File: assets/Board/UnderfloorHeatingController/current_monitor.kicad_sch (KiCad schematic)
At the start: 15 parts, among them U1 BL0937B

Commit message: Fully routed board.
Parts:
- added C19: 0.1uF, Capacitor_SMD:C_0805_2012Metric_Pad1.18x1.45mm_HandSolder, symbol Device:C
- added C20: 10uF, Capacitor_SMD:C_0805_2012Metric_Pad1.18x1.45mm_HandSolder, symbol Device:C
- C2, C4, C6: value 68n -> 68nF
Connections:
- net +3V3: now also C19.1, C20.1
- net GND: now also C19.2, C20.2
- net POWER_N: now also R11.4; no longer R11.1, R11.2, R2.1
- net POWER_N_MON: now also R11.1; no longer R11.3, R11.4, R3.1
- net at C4.2, R3.2: now also U1.3 (IN); no longer U1.2 (IP)
- net at C2.1, R2.2: now also U1.2 (IP); no longer U1.3 (IN)
- new net MON_CURRENT_SENSE_1: R11.3, R2.1
- new net MON_CURRENT_SENSE_2: R11.2, R3.1
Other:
- moved on the sheet: R11

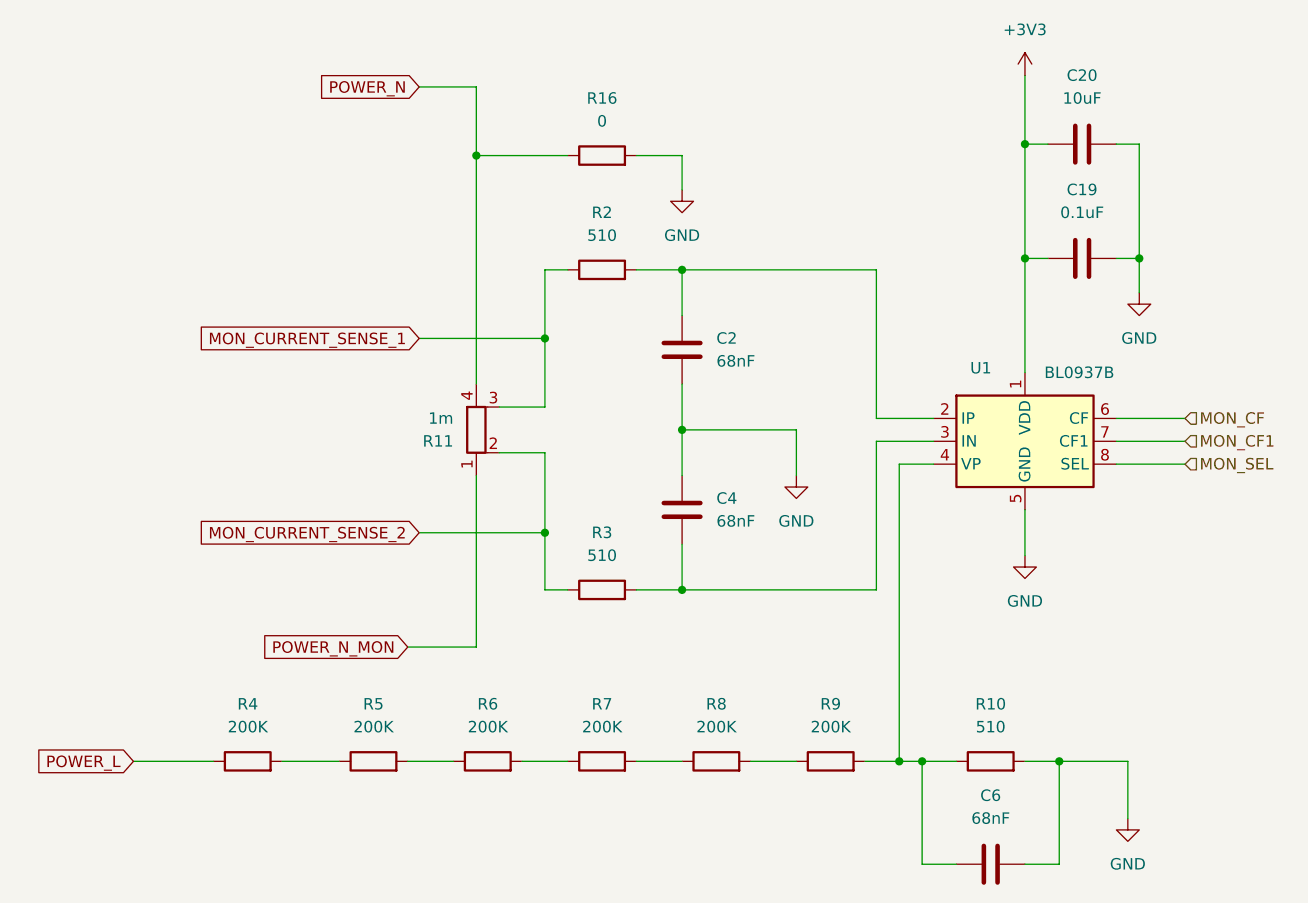
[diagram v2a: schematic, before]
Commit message: Corrected current monitor lines.
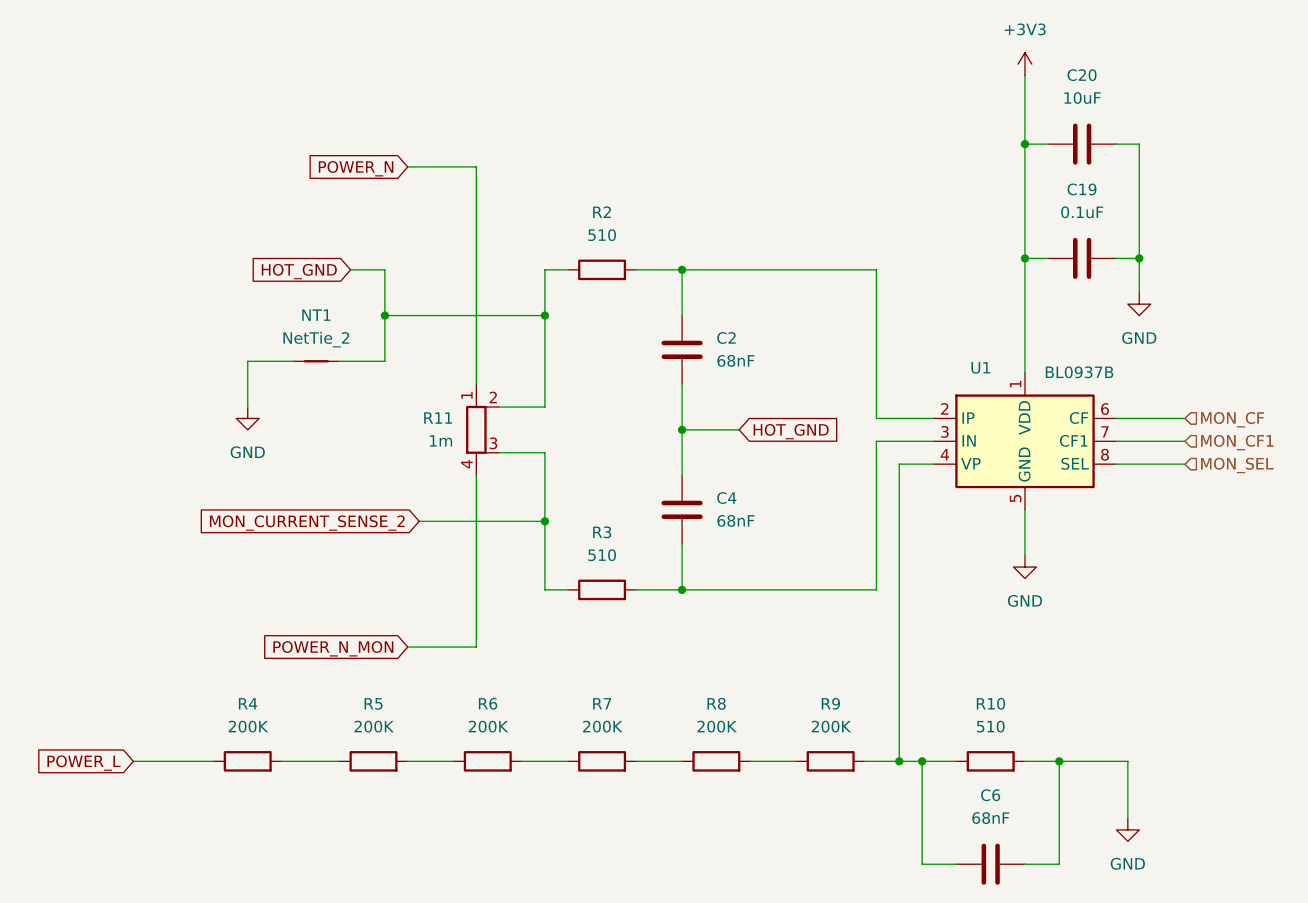
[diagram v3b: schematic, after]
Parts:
- removed R16: 0, Resistor_SMD:R_0805_2012Metric_Pad1.20x1.40mm_HandSolder, symbol Device:R
- added NT1: NetTie_2, NetTie:NetTie-2_SMD_Pad0.5mm, symbol Device:NetTie_2
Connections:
- net GND: now also NT1.1; no longer C2.2, C4.1
- net MON_CURRENT_SENSE_2: now also R11.3; no longer R11.2
- net POWER_N: now also R11.1; no longer R11.4
- net POWER_N_MON: now also R11.4; no longer R11.1
- net MON_CURRENT_SENSE_1 renamed HOT_GND
- net HOT_GND: now also C2.2, C4.1, R11.2, NT1.2; no longer R11.3

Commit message: Layout fixes.
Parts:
- R4, R5, R6, R7, R8, R9: footprint Resistor_SMD:R_1206_3216Metric_Pad1.30x1.75mm_HandSolder -> Resistor_SMD:R_0805_2012Metric_Pad1.20x1.40mm_HandSolder
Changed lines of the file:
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@@
 			)
 		)
-		(property "Footprint" "Resistor_SMD:R_1206_3216Metric_Pad1.30x1.75mm_HandSolder"
+		(property "Footprint" "Resistor_SMD:R_0805_2012Metric_Pad1.20x1.40mm_HandSolder"
 			(at 64.77 131.318 90)
 			(effects
@@
 			)
 		)
-		(property "Footprint" "Resistor_SMD:R_1206_3216Metric_Pad1.30x1.75mm_HandSolder"
+		(property "Footprint" "Resistor_SMD:R_0805_2012Metric_Pad1.20x1.40mm_HandSolder"
 			(at 104.14 131.318 90)
 			(effects
@@
 			)
 		)
-		(property "Footprint" "Resistor_SMD:R_1206_3216Metric_Pad1.30x1.75mm_HandSolder"
+		(property "Footprint" "Resistor_SMD:R_0805_2012Metric_Pad1.20x1.40mm_HandSolder"
 			(at 78.74 131.318 90)
 			(effects
@@
 			)
 		)
-		(property "Footprint" "Resistor_SMD:R_1206_3216Metric_Pad1.30x1.75mm_HandSolder"
+		(property "Footprint" "Resistor_SMD:R_0805_2012Metric_Pad1.20x1.40mm_HandSolder"
 			(at 91.44 131.318 90)
 			(effects
@@
 			)
 		)
-		(property "Footprint" "Resistor_SMD:R_1206_3216Metric_Pad1.30x1.75mm_HandSolder"
+		(property "Footprint" "Resistor_SMD:R_0805_2012Metric_Pad1.20x1.40mm_HandSolder"
 			(at 116.84 131.318 90)
 			(effects
@@
 			)
 		)
-		(property "Footprint" "Resistor_SMD:R_1206_3216Metric_Pad1.30x1.75mm_HandSolder"
+		(property "Footprint" "Resistor_SMD:R_0805_2012Metric_Pad1.20x1.40mm_HandSolder"
 			(at 129.54 131.318 90)
 			(effects
